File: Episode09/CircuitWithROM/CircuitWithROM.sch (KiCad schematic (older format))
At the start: 20 parts, among them SW101 SW_Push, U101 MAX708, U102 HD6809, U103 74HCT00, U104 74HCT27, U105 74HCT138, U106 74HCT138, U107 74HCT138, U108 27C512, Y101 Crystal

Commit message: added output port and 7 segment display
The output port (74HCT574) requires an OR gate to generate
its clock pulse, which unfortunately required another
IC (74HCT32).  This hardware probably won't be used in
the final circuit, however.
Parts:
- removed unit 3 of U104
- added AFF101: LTS-6960HR, Display_7Segment:7SegmentLED_LTS6760_LTS6780, symbol Display_Character:LTS-6960HR
- added C109: 0.1 uF, symbol device:C
- added R102, R103, R104, R105, R106, R107, R108, R109: R, symbol device:R
- added U103: 74HCT27, symbol 74xx:74LS27
- added U109: 74HCT574, symbol 74xx:74LS574
- added U110: 74HCT32, symbol 74xx:74LS32
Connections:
- net labels added: R~W~, ~IODEV0~
- wire segments 231 -> 298
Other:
- note added: "6809 circuit with glue logic, ROM, and output port"
- note added: "This is a temporary output port\nand 7 segment LED display to be\nused for testing. They will (most\nlikely) be removed in the next\nversion of the circuit (along with\nthe OR gate needed to decode\nR~W~ and ~IODEV0~.)"
- note added: "Unused gates"
- note removed: "6809 circuit with glue logic and ROM"
- moved on the sheet: C104, C105, C106, C107, C108, U103E, U104D, U108

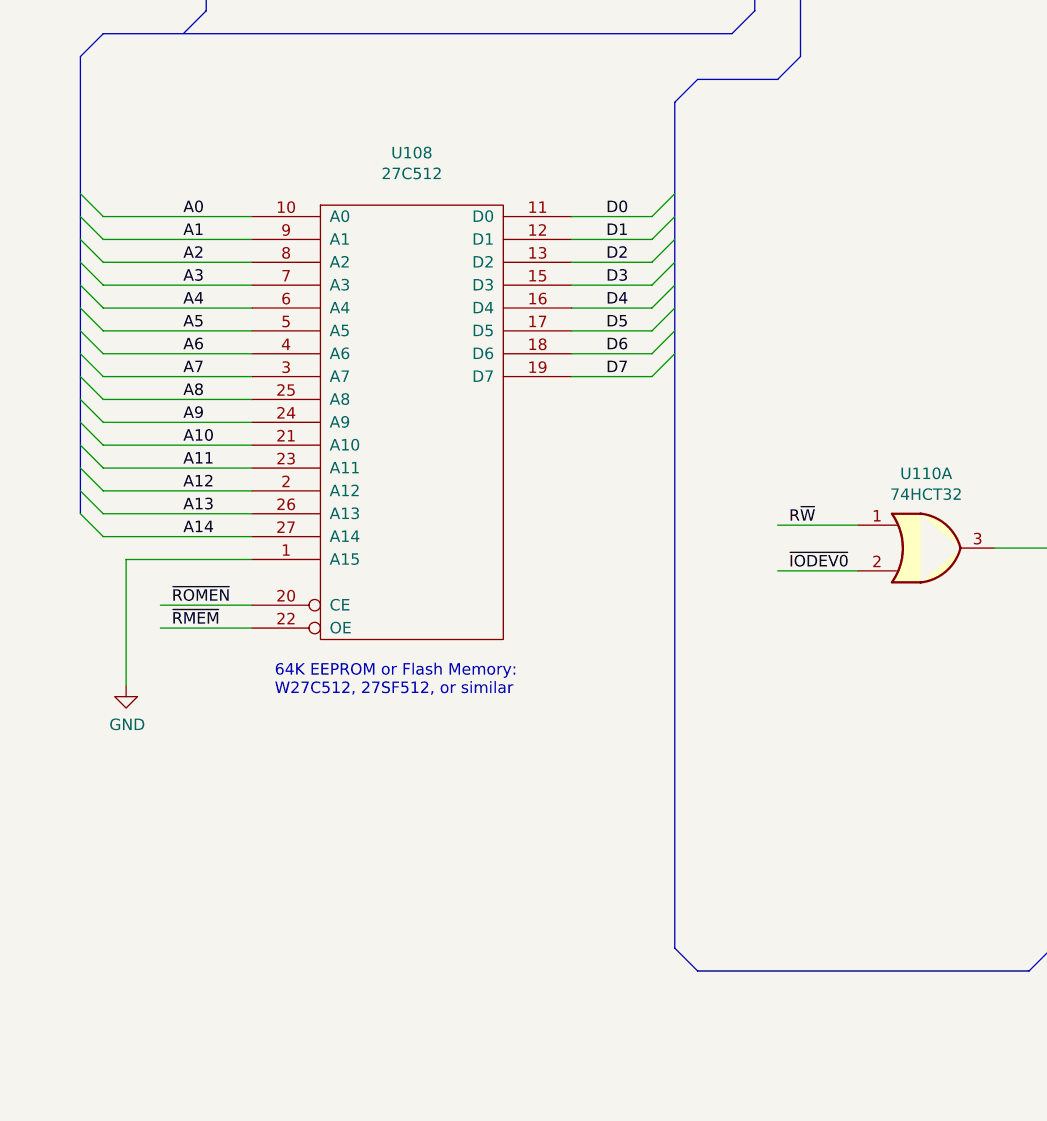
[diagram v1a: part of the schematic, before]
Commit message: change ROM to 28C256, fix control of port
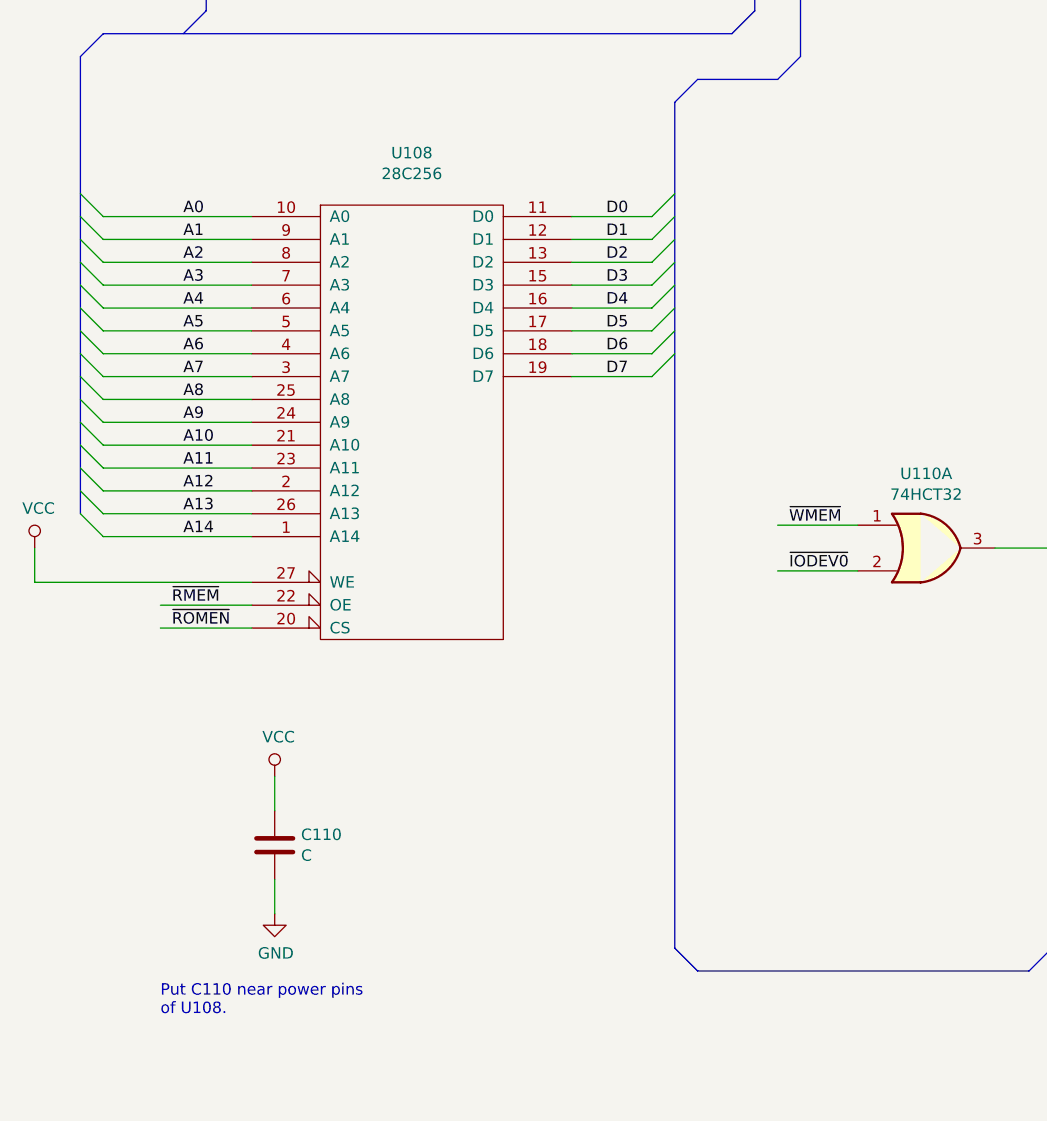
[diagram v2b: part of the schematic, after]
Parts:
- removed U108: 27C512, symbol memory:27C512
- added C110: C, symbol device:C
- added U108: 28C256, symbol memory:28C256
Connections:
- net labels added: ~WMEM~
- net labels removed: R~W~
- wire segments 298 -> 300
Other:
- note added: "Put C110 near power pins\nof U108."
- note removed: "64K EEPROM or Flash Memory:\nW27C512, 27SF512, or similar"
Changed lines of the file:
@@
 Text Label 3550 5150 0    50   ~ 0
 D7
-$Comp
-L memory:27C512 U108
-U 1 1 5CA69FAE
-P 2350 7500
-F 0 "U108" H 2350 8678 50  0000 C CNN
-F 1 "27C512" H 2350 8587 50  0000 C CNN
-F 2 "" H 2350 7500 50  0001 C CNN
-F 3 "" H 2350 7500 50  0001 C CNN
-	1    2350 7500
-	1    0    0    -1
-$EndComp
 Wire Wire Line
 	1650 6600 1000 6600
@@
 	1650 8000 1000 8000
 Wire Wire Line
-	1650 8100 1100 8100
+	1650 8200 700  8200
 Text Label 1350 6600 0    50   ~ 0
 A0
@@
 A14
 Wire Wire Line
-	1100 8100 1100 8650
-$Comp
-L power:GND #PWR?
-U 1 1 5CA83A54
-P 1100 8650
-F 0 "#PWR?" H 1100 8400 50  0001 C CNN
-F 1 "GND" H 1105 8477 50  0000 C CNN
-F 2 "" H 1100 8650 50  0001 C CNN
-F 3 "" H 1100 8650 50  0001 C CNN
-	1    1100 8650
-	1    0    0    -1
-$EndComp
-Wire Wire Line
 	3050 6600 3400 6600
 Wire Wire Line
@@
 D7
 Wire Wire Line
+	1650 8400 1250 8400
+Wire Wire Line
 	1650 8300 1250 8300
-Wire Wire Line
-	1650 8400 1250 8400
+Text Label 1300 8400 0    50   ~ 0
+~ROMEN~
 Text Label 1300 8300 0    50   ~ 0
-~ROMEN~
-Text Label 1300 8400 0    50   ~ 0
 ~RMEM~
-Text Notes 1750 8700 0    50   ~ 0
-64K EEPROM or Flash Memory:\nW27C512, 27SF512, or similar
 Wire Wire Line
 	1900 4250 1550 4250
@@
 Wire Wire Line
 	4300 8150 3950 8150
-Text Label 4000 7950 0    50   ~ 0
-R~W~
 Text Label 4000 8150 0    50   ~ 0
 ~IODEV0~
@@
 	1    0    0    -1
 $EndComp
+Text Label 4000 7950 0    50   ~ 0
+~WMEM~
+$Comp
+L memory:28C256 U108
+U 1 1 5CAEF11C
+P 2350 7500
+F 0 "U108" H 2350 8678 50  0000 C CNN
+F 1 "28C256" H 2350 8587 50  0000 C CNN
+F 2 "" H 2350 7500 50  0001 C CNN
+F 3 "" H 2350 7500 50  0001 C CNN
+	1    2350 7500
+	1    0    0    -1
+$EndComp
+Wire Wire Line
+	700  8050 700  8200
+$Comp
+L power:VCC #PWR?
+U 1 1 5CBAF808
+P 700 8050
+F 0 "#PWR?" H 700 7900 50  0001 C CNN
+F 1 "VCC" H 717 8223 50  0000 C CNN
+F 2 "" H 700 8050 50  0001 C CNN
+F 3 "" H 700 8050 50  0001 C CNN
+	1    700  8050
+	1    0    0    -1
+$EndComp
+$Comp
+L device:C C110
+U 1 1 5CBB0670
+P 1750 9350
+F 0 "C110" H 1865 9396 50  0000 L CNN
+F 1 "C" H 1865 9305 50  0000 L CNN
+F 2 "" H 1788 9200 50  0001 C CNN
+F 3 "" H 1750 9350 50  0001 C CNN
+	1    1750 9350
+	1    0    0    -1
+$EndComp
+Wire Wire Line
+	1750 9200 1750 9050
+Wire Wire Line
+	1750 9650 1750 9500
 Wire Bus Line
 	1000 5800 3750 5800
@@
 Wire Bus Line
 	900  5900 900  7900
+$Comp
+L power:VCC #PWR?
+U 1 1 5CBE8002
+P 1750 9050
+F 0 "#PWR?" H 1750 8900 50  0001 C CNN
+F 1 "VCC" H 1767 9223 50  0000 C CNN
+F 2 "" H 1750 9050 50  0001 C CNN
+F 3 "" H 1750 9050 50  0001 C CNN
+	1    1750 9050
+	1    0    0    -1
+$EndComp
+$Comp
+L power:GND #PWR?
+U 1 1 5CBE80E7
+P 1750 9650
+F 0 "#PWR?" H 1750 9400 50  0001 C CNN
+F 1 "GND" H 1755 9477 50  0000 C CNN
+F 2 "" H 1750 9650 50  0001 C CNN
+F 3 "" H 1750 9650 50  0001 C CNN
+	1    1750 9650
+	1    0    0    -1
+$EndComp
+Text Notes 1250 10100 0    50   ~ 0
+Put C110 near power pins\nof U108.
 $EndSCHEMATC
